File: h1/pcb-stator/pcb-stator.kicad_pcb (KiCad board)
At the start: 2 copper layers, 92.7 x 126.3 mm, 1646 parts, among them J1 Conn_01x01_Pin

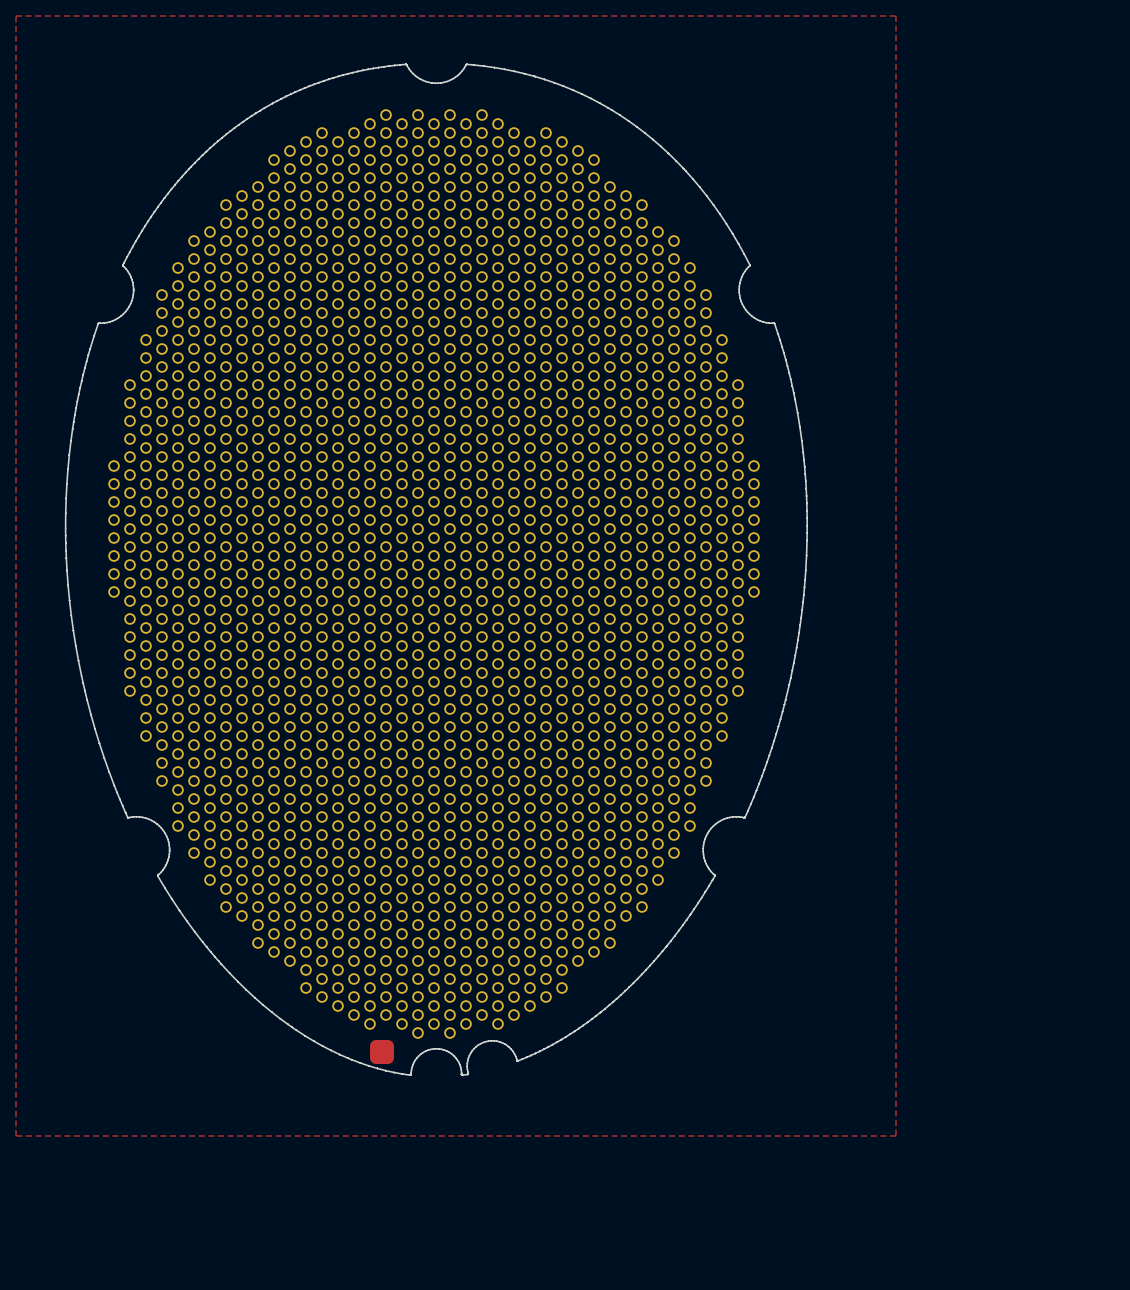
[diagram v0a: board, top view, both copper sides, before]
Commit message: h1: fixed stator alignment
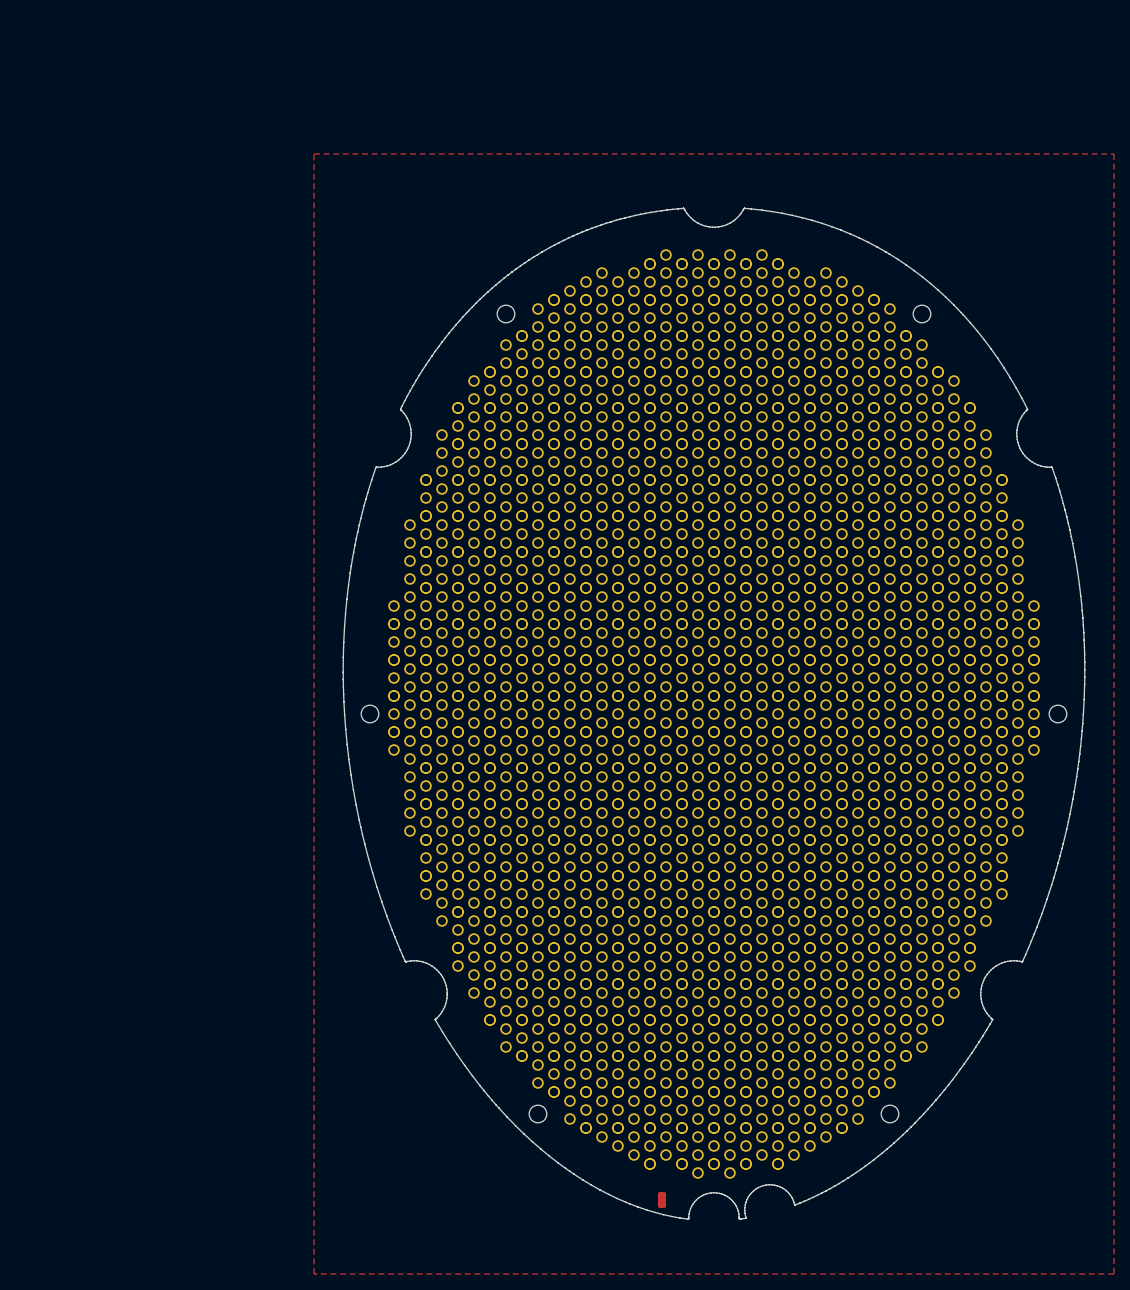
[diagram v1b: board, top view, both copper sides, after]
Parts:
- removed the ? at (41.0, 69.0)
- removed the ? at (81.0, 105.0)
- removed the ? at (45.0, 89.2)
- removed the ? at (67.0, 70.1)
- removed the ? at (37.0, 78.0)
- removed the ? at (71.0, 106.1)
- removed the ? at (37.0, 80.2)
- removed the ? at (45.0, 33.0)
- removed the ? at (73.0, 125.2)
- removed the ? at (77.0, 80.2)
- removed the ? at (65.0, 26.2)
- removed the ? at (49.0, 69.0)
- removed the ? at (61.0, 60.0)
- removed the ? at (61.0, 71.2)
- removed the ? at (73.0, 132.0)
- removed the ? at (61.0, 132.0)
- removed the ? at (91.0, 70.1)
- removed the ? at (81.0, 62.2)
- removed the ? at (95.0, 67.9)
- removed the ? at (59.0, 94.9)
- removed the ? at (41.0, 44.2)
- removed the ? at (81.0, 98.2)
- removed the ? at (55.0, 40.9)
- removed the ? at (61.0, 80.2)
- removed the ? at (63.0, 49.9)
- removed the ? at (93.0, 71.2)
- removed the ? at (91.0, 58.9)
- removed the ? at (89.0, 80.2)
- removed the ? at (55.0, 85.9)
- removed the ? at (59.0, 124.1)
- removed the ? at (39.0, 79.1)
- removed the ? at (77.0, 107.2)
- removed the ? at (67.0, 31.9)
- removed the ? at (37.0, 116.2)
- removed the ? at (83.0, 130.9)
- removed the ? at (75.0, 121.9)
- removed the ? at (59.0, 67.9)
- removed the ? at (33.0, 96.0)
- removed the ? at (57.0, 80.2)
- removed the ? at (95.0, 52.1)
- removed the ? at (87.0, 124.1)
- removed the ? at (99.0, 61.1)
- removed the ? at (63.0, 43.1)
- removed the ? at (65.0, 53.2)
- removed the ? at (93.0, 87.0)
- removed the ? at (53.0, 44.2)
- removed the ? at (89.0, 62.2)
- removed the ? at (75.0, 58.9)
- removed the ? at (59.0, 103.9)
- removed the ? at (41.0, 51.0)
- removed the ? at (101.0, 69.0)
- removed the ? at (41.0, 80.2)
- removed the ? at (53.0, 51.0)
- removed the ? at (89.0, 123.0)
- removed the ? at (75.0, 61.1)
- removed the ? at (65.0, 132.0)
- removed the ? at (53.0, 78.0)
- removed the ? at (41.0, 62.2)
- removed the ? at (71.0, 76.9)
- removed the ? at (27.0, 67.9)
- removed the ? at (91.0, 94.9)
- removed the ? at (53.0, 134.2)
- removed the ? at (97.0, 78.0)
- removed the ? at (67.0, 124.1)
- removed the ? at (47.0, 88.1)
- removed the ? at (85.0, 78.0)
- removed the ? at (71.0, 34.1)
- removed the ? at (79.0, 76.9)
- removed the ? at (83.0, 34.1)
- removed the ? at (63.0, 88.1)
- removed the ? at (89.0, 96.0)
- removed the ? at (79.0, 121.9)
- removed the ? at (57.0, 116.2)
- removed the ? at (101.0, 96.0)
- removed the ? at (69.0, 42.0)
- removed the ? at (47.0, 97.1)
- removed the ? at (53.0, 87.0)
- removed the ? at (49.0, 53.2)
- removed the ? at (53.0, 107.2)
- removed the ? at (43.0, 115.1)
- removed the ? at (67.0, 133.1)
- removed the ? at (55.0, 115.1)
- removed the ? at (89.0, 89.2)
- removed the ? at (99.0, 52.1)
- removed the ? at (97.0, 62.2)
- removed the ? at (57.0, 44.2)
- removed the ? at (69.0, 71.2)
- removed the ? at (31.0, 49.9)
- removed the ? at (39.0, 115.1)
- removed the ? at (41.0, 123.0)
- removed the ? at (75.0, 97.1)
- removed the ? at (31.0, 70.1)
- removed the ? at (79.0, 49.9)
- removed the ? at (105.0, 80.2)
- removed the ? at (99.0, 70.1)
- removed the ? at (91.0, 52.1)
- removed the ? at (95.0, 94.9)
- removed the ? at (83.0, 79.1)
- removed the ? at (69.0, 132.0)
- removed the ? at (73.0, 51.0)
- removed the ? at (57.0, 51.0)
- removed the ? at (51.0, 79.1)
- removed the ? at (39.0, 106.1)
- removed the ? at (51.0, 112.9)
- removed the ? at (99.0, 67.9)
- removed the ? at (93.0, 116.2)
- removed the ? at (91.0, 40.9)
- removed the ? at (55.0, 34.1)
- removed the ? at (83.0, 112.9)
- removed the ? at (43.0, 49.9)
- removed the ? at (73.0, 78.0)
- removed the ? at (37.0, 105.0)
- removed the ? at (59.0, 43.1)
- removed the ? at (31.0, 103.9)
- removed the ? at (77.0, 78.0)
- removed the ? at (81.0, 132.0)
- removed the ? at (85.0, 62.2)
- removed the ? at (29.0, 71.2)
- removed the ? at (35.0, 85.9)
- removed the ? at (49.0, 123.0)
- removed the ? at (59.0, 34.1)
- removed the ? at (67.0, 61.1)
- removed the ? at (79.0, 97.1)
- removed the ? at (59.0, 121.9)
- removed the ? at (35.0, 52.1)
- removed the ? at (37.0, 60.0)
- removed the ? at (73.0, 134.2)
- removed the ? at (55.0, 52.1)
- removed the ? at (99.0, 76.9)
- removed the ? at (67.0, 112.9)
- removed the ? at (103.0, 88.1)
- removed the ? at (87.0, 49.9)
- removed the ? at (43.0, 34.1)
- removed the ? at (71.0, 25.1)
- removed the ? at (63.0, 40.9)
- removed the ? at (65.0, 42.0)
- removed the ? at (47.0, 61.1)
- removed the ? at (73.0, 98.2)
- removed the ? at (27.0, 76.9)
- removed the ? at (47.0, 52.1)
- removed the ? at (49.0, 35.2)
- removed the ? at (83.0, 49.9)
- removed the ? at (81.0, 53.2)
- removed the ? at (61.0, 105.0)
- removed the ? at (65.0, 78.0)
- removed the ? at (105.0, 78.0)
- removed the ? at (61.0, 69.0)
- removed the ? at (53.0, 105.0)
- removed the ? at (65.0, 116.2)
- removed the ? at (69.0, 44.2)
- removed the ? at (81.0, 107.2)
- removed the ? at (67.0, 139.9)
- removed the ? at (103.0, 79.1)
- removed the ? at (65.0, 123.0)
- removed the ? at (103.0, 85.9)
- removed the ? at (105.0, 69.0)
- removed the ? at (61.0, 35.2)
- removed the ? at (53.0, 125.2)
- removed the ? at (69.0, 35.2)
- removed the ? at (65.0, 51.0)
- removed the ? at (41.0, 71.2)
- removed the ? at (47.0, 106.1)
- removed the ? at (99.0, 85.9)
- removed the ? at (77.0, 51.0)
- removed the ? at (65.0, 62.2)
- removed the ? at (63.0, 76.9)
- removed the ? at (79.0, 79.1)
- removed the ? at (69.0, 69.0)
- removed the ? at (81.0, 69.0)
- removed the ? at (35.0, 88.1)
- removed the ? at (55.0, 94.9)
- removed the ? at (65.0, 114.0)
- removed the ? at (55.0, 43.1)
- removed the ? at (49.0, 116.2)
- removed the ? at (61.0, 78.0)
- removed the ? at (71.0, 70.1)
- removed the ? at (75.0, 76.9)
- removed the ? at (87.0, 121.9)
- removed the ? at (61.0, 96.0)
- removed the ? at (81.0, 33.0)
- removed the ? at (45.0, 69.0)
- removed the ? at (95.0, 88.1)
- removed the ? at (27.0, 79.1)
- removed the ? at (73.0, 123.0)
- removed the ? at (79.0, 112.9)
- removed the ? at (55.0, 61.1)
- removed the ? at (53.0, 71.2)
- removed the ? at (71.0, 61.1)
- removed the ? at (55.0, 133.1)
- removed the ? at (31.0, 58.9)
- removed the ? at (47.0, 34.1)
- removed the ? at (33.0, 44.2)
- removed the ? at (57.0, 123.0)
- removed the ? at (79.0, 115.1)
- removed the ? at (99.0, 106.1)
- removed the ? at (81.0, 89.2)
- removed the ? at (37.0, 69.0)
- removed the ? at (41.0, 60.0)
- removed the ? at (73.0, 89.2)
- removed the ? at (97.0, 89.2)
- removed the ? at (61.0, 53.2)
- removed the ? at (101.0, 71.2)
- removed the ? at (49.0, 78.0)
- removed the ? at (41.0, 35.2)
- removed the ? at (55.0, 121.9)
- removed the ? at (35.0, 106.1)
- removed the ? at (31.0, 94.9)
- removed the ? at (93.0, 114.0)
- removed the ? at (45.0, 51.0)
- removed the ? at (85.0, 42.0)
- removed the ? at (57.0, 132.0)
- removed the ? at (95.0, 49.9)
- removed the ? at (51.0, 130.9)
- removed the ? at (71.0, 124.1)
- removed the ? at (95.0, 97.1)
- removed the ? at (47.0, 112.9)
- removed the ? at (93.0, 80.2)
- removed the ? at (97.0, 60.0)
- removed the ? at (83.0, 94.9)
- removed the ? at (89.0, 35.2)
- removed the ? at (77.0, 105.0)
- removed the ? at (87.0, 88.1)
- removed the ? at (83.0, 121.9)
- removed the ? at (85.0, 87.0)
- removed the ? at (27.0, 58.9)
- removed the ? at (45.0, 87.0)
- removed the ? at (43.0, 121.9)
- removed the ? at (79.0, 34.1)
- removed the ? at (51.0, 121.9)
- removed the ? at (43.0, 106.1)
- removed the ? at (81.0, 116.2)
- removed the ? at (51.0, 34.1)
- removed the ? at (31.0, 106.1)
- removed the ? at (55.0, 58.9)
- removed the ? at (89.0, 69.0)
- removed the ? at (65.0, 80.2)
- removed the ? at (39.0, 103.9)
- removed the ? at (97.0, 107.2)
- removed the ? at (33.0, 107.2)
- removed the ? at (75.0, 43.1)
- removed the ? at (71.0, 85.9)
- removed the ? at (69.0, 125.2)
- removed the ? at (73.0, 44.2)
- removed the ? at (61.0, 107.2)
- removed the ? at (75.0, 52.1)
- removed the ? at (63.0, 97.1)
- removed the ? at (37.0, 62.2)
- removed the ? at (83.0, 31.9)
- removed the ? at (67.0, 106.1)
- removed the ? at (91.0, 112.9)
- removed the ? at (59.0, 58.9)
- removed the ? at (87.0, 67.9)
- removed the ? at (31.0, 85.9)
- removed the ? at (89.0, 44.2)
- removed the ? at (73.0, 69.0)
- removed the ? at (71.0, 67.9)
- removed the ? at (69.0, 107.2)
- removed the ? at (67.0, 79.1)
- removed the ? at (91.0, 43.1)
- removed the ? at (63.0, 31.9)
- removed the ? at (81.0, 44.2)
- removed the ? at (61.0, 98.2)
- removed the ? at (85.0, 105.0)
- removed the ? at (71.0, 121.9)
- removed the ? at (71.0, 40.9)
- removed the ? at (61.0, 116.2)
- removed the ? at (47.0, 130.9)
- removed the ? at (81.0, 71.2)
- removed the ? at (65.0, 35.2)
- removed the ? at (87.0, 112.9)
- removed the ? at (93.0, 105.0)
- removed the ? at (83.0, 43.1)
- removed the ? at (101.0, 87.0)
- removed the ? at (87.0, 52.1)
- removed the ? at (67.0, 40.9)
- removed the ? at (59.0, 115.1)
- removed the ? at (43.0, 79.1)
- removed the ? at (67.0, 103.9)
- removed the ? at (65.0, 60.0)
- removed the ? at (63.0, 58.9)
- removed the ? at (25.0, 78.0)
- removed the ? at (59.0, 79.1)
- removed the ? at (101.0, 80.2)
- removed the ? at (53.0, 89.2)
- removed the ? at (51.0, 61.1)
- removed the ? at (69.0, 89.2)
- removed the ? at (59.0, 31.9)
- removed the ? at (73.0, 105.0)
- removed the ? at (41.0, 114.0)
- removed the ? at (97.0, 53.2)
- removed the ? at (39.0, 88.1)
- removed the ? at (53.0, 60.0)
- removed the ? at (53.0, 42.0)
- removed the ? at (35.0, 79.1)
- removed the ? at (47.0, 43.1)
- removed the ? at (51.0, 94.9)
- removed the ? at (93.0, 60.0)
- removed the ? at (69.0, 78.0)
- removed the ? at (61.0, 87.0)
- removed the ? at (83.0, 70.1)
- removed the ? at (59.0, 40.9)
- removed the ? at (97.0, 96.0)
- removed the ? at (63.0, 103.9)
- removed the ? at (89.0, 42.0)
- removed the ? at (79.0, 61.1)
- removed the ? at (45.0, 71.2)
- removed the ? at (85.0, 71.2)
- removed the ? at (83.0, 67.9)
- removed the ? at (51.0, 124.1)
- removed the ? at (37.0, 89.2)
- removed the ? at (35.0, 40.9)
- removed the ? at (95.0, 106.1)
- removed the ? at (99.0, 94.9)
- removed the ? at (55.0, 49.9)
- removed the ? at (57.0, 105.0)
- removed the ? at (77.0, 123.0)
- removed the ? at (51.0, 49.9)
- removed the ? at (35.0, 76.9)
- removed the ? at (47.0, 94.9)
- removed the ? at (65.0, 98.2)
- removed the ? at (49.0, 107.2)
- removed the ? at (45.0, 60.0)
- removed the ? at (31.0, 61.1)
- removed the ? at (89.0, 71.2)
- removed the ? at (55.0, 67.9)
- removed the ? at (61.0, 125.2)
- removed the ? at (47.0, 85.9)
- removed the ? at (47.0, 121.9)
- removed the ? at (29.0, 53.2)
- removed the ? at (63.0, 112.9)
- removed the ? at (31.0, 52.1)
- removed the ? at (35.0, 97.1)
- removed the ? at (49.0, 44.2)
- removed the ? at (59.0, 133.1)
- removed the ? at (51.0, 88.1)
- removed the ? at (97.0, 51.0)
- removed the ? at (27.0, 61.1)
- removed the ? at (43.0, 85.9)
- removed the ? at (29.0, 62.2)
- removed the ? at (73.0, 60.0)
- removed the ? at (57.0, 26.2)
- removed the ? at (91.0, 61.1)
- removed the ? at (81.0, 134.2)
- removed the ? at (77.0, 62.2)
- removed the ? at (69.0, 60.0)
- removed the ? at (43.0, 40.9)
- removed the ? at (39.0, 94.9)
- removed the ? at (41.0, 89.2)
- removed the ? at (69.0, 26.2)
- removed the ? at (31.0, 88.1)
- removed the ? at (95.0, 61.1)
- removed the ? at (33.0, 114.0)
- removed the ? at (73.0, 116.2)
- removed the ? at (91.0, 79.1)
- removed the ? at (91.0, 67.9)
- removed the ? at (53.0, 69.0)
- removed the ? at (51.0, 43.1)
- removed the ? at (59.0, 112.9)
- removed the ? at (97.0, 87.0)
- removed the ? at (49.0, 98.2)
- removed the ? at (83.0, 40.9)
- removed the ? at (55.0, 103.9)
- removed the ? at (53.0, 116.2)
- removed the ? at (33.0, 87.0)
- removed the ? at (61.0, 51.0)
- removed the ? at (69.0, 116.2)
- removed the ? at (71.0, 94.9)
- removed the ? at (89.0, 114.0)
- removed the ? at (49.0, 134.2)
- removed the ? at (91.0, 97.1)
- removed the ? at (35.0, 70.1)
- removed the ? at (83.0, 106.1)
- removed the ? at (45.0, 107.2)
- removed the ? at (51.0, 97.1)
- removed the ? at (51.0, 52.1)
- removed the ? at (71.0, 133.1)
- removed the ? at (99.0, 58.9)
- removed the ? at (29.0, 98.2)
- removed the ? at (65.0, 69.0)
- removed the ? at (51.0, 58.9)
- removed the ? at (45.0, 53.2)
- removed the ? at (83.0, 52.1)
- removed the ? at (91.0, 121.9)
- removed the ? at (39.0, 112.9)
- removed the ? at (103.0, 70.1)
- removed the ? at (53.0, 98.2)
- removed the ? at (75.0, 130.9)
- removed the ? at (85.0, 51.0)
- removed the ? at (101.0, 98.2)
- removed the ? at (69.0, 80.2)
- removed the ? at (39.0, 61.1)
- removed the ? at (53.0, 114.0)
- removed the ? at (65.0, 71.2)
- removed the ? at (69.0, 105.0)
- removed the ? at (47.0, 70.1)
- removed the ? at (91.0, 106.1)
- removed the ? at (65.0, 89.2)
- removed the ? at (41.0, 96.0)
- removed the ? at (57.0, 53.2)
- removed the ? at (37.0, 42.0)
- removed the ? at (95.0, 70.1)
- removed the ? at (103.0, 61.1)
- removed the ? at (103.0, 76.9)
- removed the ? at (79.0, 103.9)
- removed the ? at (75.0, 79.1)
- removed the ? at (99.0, 79.1)
- removed the ? at (97.0, 105.0)
- removed the ? at (73.0, 35.2)
- removed the ? at (71.0, 49.9)
- removed the ? at (75.0, 103.9)
- removed the ? at (93.0, 107.2)
- removed the ? at (41.0, 107.2)
- removed the ? at (33.0, 62.2)
- removed the ? at (35.0, 67.9)
- removed the ? at (27.0, 94.9)
- removed the ? at (63.0, 115.1)
- removed the ? at (93.0, 44.2)
- removed the ? at (57.0, 62.2)
- removed the ? at (45.0, 105.0)
- removed the ? at (77.0, 87.0)
- removed the ? at (47.0, 58.9)
- removed the ? at (59.0, 88.1)
- removed the ? at (47.0, 76.9)
- removed the ? at (75.0, 133.1)
- removed the ? at (81.0, 78.0)
- removed the ? at (63.0, 52.1)
- removed the ? at (77.0, 134.2)
- removed the ? at (67.0, 130.9)
- removed the ? at (85.0, 80.2)
- removed the ? at (99.0, 97.1)
- removed the ? at (69.0, 62.2)
- removed the ? at (61.0, 42.0)
- removed the ? at (63.0, 106.1)
- removed the ? at (33.0, 105.0)
- removed the ? at (59.0, 52.1)
- removed the ? at (83.0, 97.1)
- removed the ? at (39.0, 43.1)
- removed the ? at (79.0, 52.1)
- removed the ? at (37.0, 44.2)
- removed the ? at (93.0, 42.0)
- removed the ? at (39.0, 49.9)
- removed the ? at (55.0, 112.9)
- removed the ? at (95.0, 43.1)
- removed the ? at (79.0, 124.1)
- removed the ? at (69.0, 51.0)
- removed the ? at (63.0, 70.1)
- removed the ? at (63.0, 34.1)
- removed the ? at (43.0, 61.1)
- removed the ? at (31.0, 79.1)
- removed the ? at (67.0, 115.1)
- removed the ? at (103.0, 58.9)
- removed the ? at (97.0, 98.2)
- removed the ? at (33.0, 98.2)
- removed the ? at (65.0, 105.0)
- removed the ? at (53.0, 80.2)
- removed the ? at (79.0, 31.9)
- removed the ? at (87.0, 79.1)
- removed the ? at (39.0, 85.9)
- removed the ? at (45.0, 98.2)
- removed the ? at (75.0, 106.1)
- removed the ? at (85.0, 33.0)
- removed the ? at (87.0, 115.1)
- removed the ? at (71.0, 130.9)
- removed the ? at (67.0, 43.1)
- removed the ? at (49.0, 42.0)
- removed the ? at (51.0, 40.9)
- removed the ? at (57.0, 98.2)
- removed the ? at (69.0, 96.0)
- removed the ? at (85.0, 96.0)
- removed the ? at (97.0, 71.2)
- removed the ? at (87.0, 61.1)
- removed the ? at (49.0, 51.0)
- removed the ? at (79.0, 40.9)
- removed the ? at (73.0, 107.2)
- removed the ? at (67.0, 76.9)
- removed the ? at (67.0, 121.9)
- removed the ? at (49.0, 89.2)
- removed the ? at (43.0, 67.9)
- removed the ? at (101.0, 60.0)
- removed the ? at (51.0, 31.9)
- removed the ? at (53.0, 62.2)
- removed the ? at (93.0, 53.2)
- removed the ? at (49.0, 96.0)
- removed the ? at (93.0, 69.0)
- removed the ? at (83.0, 88.1)
- removed the ? at (67.0, 52.1)
- removed the ? at (99.0, 49.9)
- removed the ? at (63.0, 67.9)
- removed the ? at (71.0, 52.1)
- removed the ? at (87.0, 103.9)
- removed the ? at (85.0, 107.2)
- removed the ? at (87.0, 76.9)
- removed the ? at (97.0, 114.0)
- removed the ? at (71.0, 112.9)
- removed the ? at (57.0, 33.0)
- removed the ? at (41.0, 116.2)
- removed the ? at (53.0, 53.2)
- removed the ? at (69.0, 123.0)
- removed the ? at (83.0, 85.9)
- removed the ? at (79.0, 67.9)
- removed the ? at (49.0, 132.0)
- removed the ? at (47.0, 31.9)
- removed the ? at (87.0, 85.9)
- removed the ? at (79.0, 58.9)
- removed the ? at (65.0, 96.0)
- removed the ? at (85.0, 69.0)
- removed the ? at (77.0, 44.2)
- removed the ? at (47.0, 124.1)
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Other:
- outline, holes or cut-outs redrawn

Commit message: h1: fixed stator & spacer edge cuts
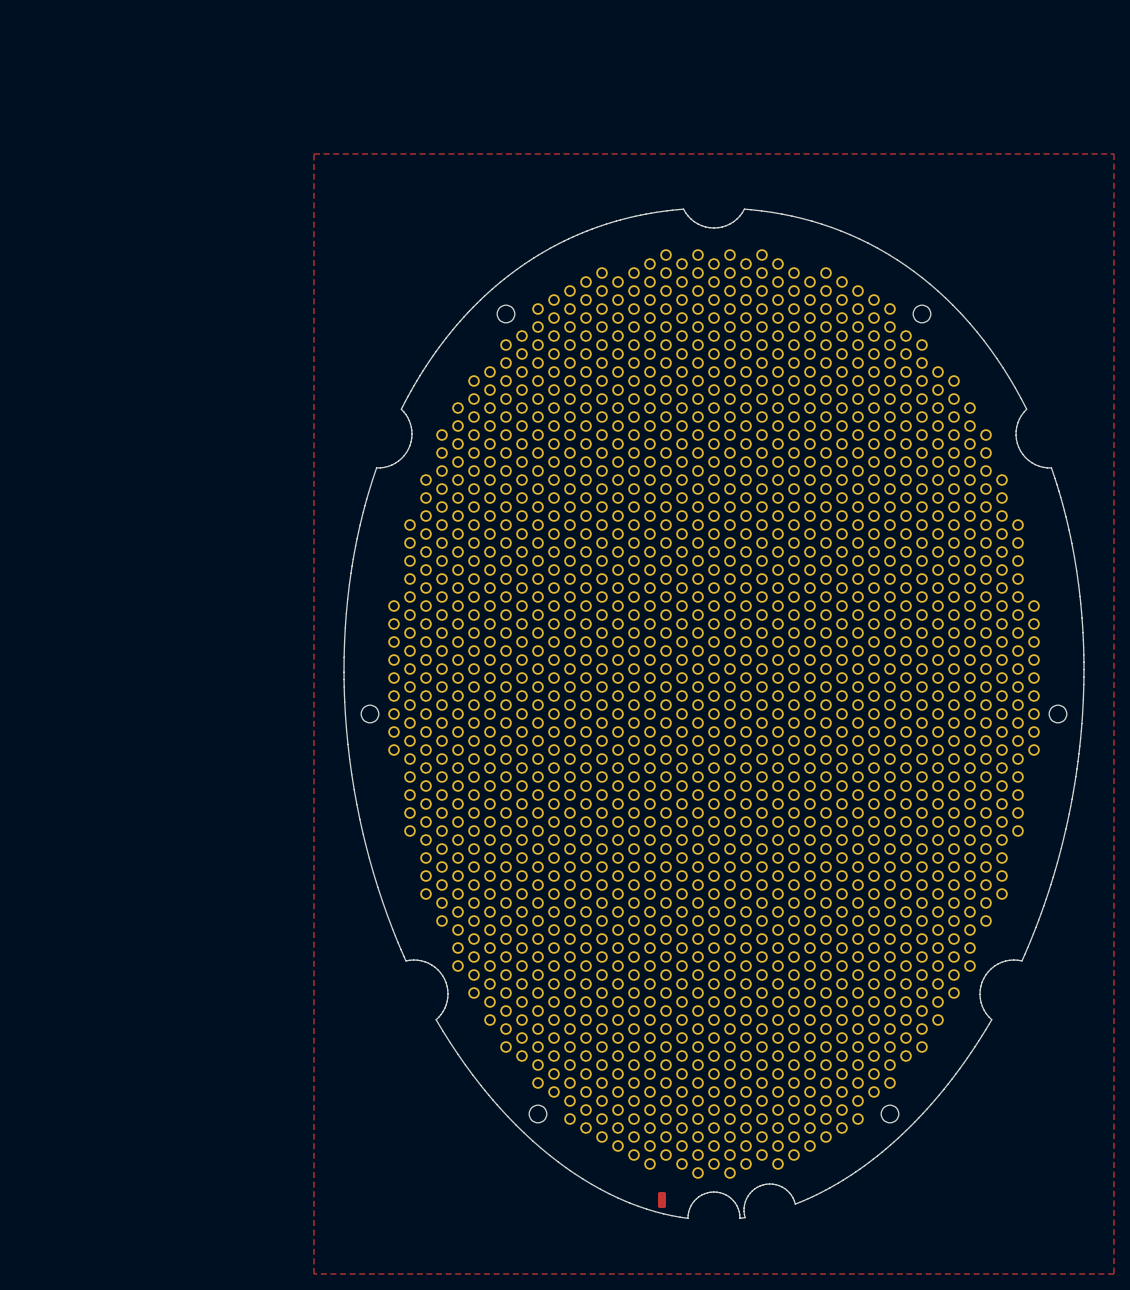
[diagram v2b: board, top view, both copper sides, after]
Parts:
- removed ? (x416): , 
- removed the REF** at (82.0, 121.4)
- removed the REF** at (92.0, 124.8)
- removed the REF** at (84.0, 95.5)
- removed the REF** at (104.0, 68.5)
- removed the REF** at (112.0, 151.8)
- removed the REF** at (114.0, 98.9)
- removed the REF** at (118.0, 76.4)
- removed the REF** at (98.0, 116.9)
- removed the REF** at (98.0, 101.1)
- removed the REF** at (102.0, 114.6)
- removed the REF** at (122.0, 80.9)
- removed the REF** at (134.0, 94.4)
- removed the REF** at (114.0, 116.9)
- removed the REF** at (98.0, 71.9)
- removed the REF** at (132.0, 127.0)
- removed the REF** at (132.0, 77.5)
- removed the REF** at (100.0, 129.2)
- removed the REF** at (118.0, 49.4)
- removed the REF** at (84.0, 75.2)
- removed the REF** at (120.0, 55.0)
- removed the REF** at (80.0, 61.8)
- removed the REF** at (116.0, 86.5)
- removed the REF** at (120.0, 145.0)
- removed the REF** at (70.0, 132.6)
- removed the REF** at (98.0, 121.4)
- removed the REF** at (116.0, 120.2)
- removed the REF** at (122.0, 51.6)
- removed the REF** at (106.0, 130.4)
- removed the REF** at (94.0, 141.6)
- removed the REF** at (70.0, 69.6)
- removed the REF** at (116.0, 124.8)
- removed the REF** at (130.0, 96.6)
- removed the REF** at (114.0, 137.1)
- removed the REF** at (126.0, 67.4)
- removed the REF** at (110.0, 155.1)
- removed the REF** at (136.0, 118.0)
- removed the REF** at (126.0, 98.9)
- removed the REF** at (110.0, 89.9)
- removed the REF** at (116.0, 151.8)
- removed the REF** at (68.0, 106.8)
- removed the REF** at (100.0, 102.2)
- removed the REF** at (96.0, 50.5)
- removed the REF** at (114.0, 89.9)
- removed the REF** at (112.0, 61.8)
- removed the REF** at (128.0, 64.0)
- removed the REF** at (86.0, 110.1)
- removed the REF** at (80.0, 64.0)
- removed the REF** at (88.0, 77.5)
- removed the REF** at (78.0, 83.1)
- removed the REF** at (118.0, 103.4)
- removed the REF** at (80.0, 133.8)
- removed the REF** at (124.0, 70.8)
- removed the REF** at (94.0, 42.6)
- removed the REF** at (108.0, 156.2)
- removed the REF** at (118.0, 87.6)
- removed the REF** at (64.0, 73.0)
- removed the REF** at (106.0, 121.4)
- removed the REF** at (118.0, 125.9)
- removed the REF** at (82.0, 65.1)
- removed the REF** at (66.0, 121.4)
- removed the REF** at (84.0, 127.0)
- removed the REF** at (122.0, 71.9)
- removed the REF** at (88.0, 97.8)
- removed the REF** at (104.0, 95.5)
- removed the REF** at (80.0, 50.5)
- removed the REF** at (96.0, 104.5)
- removed the REF** at (132.0, 118.0)
- removed the REF** at (80.0, 145.0)
- removed the REF** at (140.0, 95.5)
- removed the REF** at (120.0, 97.8)
- removed the REF** at (76.0, 91.0)
- removed the REF** at (112.0, 48.2)
- removed the REF** at (116.0, 88.8)
- removed the REF** at (104.0, 79.8)
- removed the REF** at (76.0, 52.8)
- removed the REF** at (138.0, 103.4)
- removed the REF** at (128.0, 129.2)
- removed the REF** at (98.0, 47.1)
- removed the REF** at (80.0, 79.8)
- removed the REF** at (108.0, 136.0)
- removed the REF** at (128.0, 97.8)
- removed the REF** at (102.0, 150.6)
- removed the REF** at (96.0, 52.8)
- removed the REF** at (76.0, 61.8)
- removed the REF** at (130.0, 76.4)
- removed the REF** at (98.0, 74.1)
- removed the REF** at (112.0, 70.8)
- removed the REF** at (110.0, 51.6)
- removed the REF** at (136.0, 86.5)
- removed the REF** at (74.0, 101.1)
- removed the REF** at (106.0, 85.4)
- removed the REF** at (118.0, 137.1)
- removed the REF** at (100.0, 133.8)
- removed the REF** at (94.0, 80.9)
- removed the REF** at (122.0, 69.6)
- removed the REF** at (104.0, 124.8)
- removed the REF** at (130.0, 78.6)
- removed the REF** at (84.0, 93.2)
- removed the REF** at (84.0, 100.0)
- removed the REF** at (64.0, 77.5)
- removed the REF** at (90.0, 47.1)
- removed the REF** at (106.0, 152.9)
- removed the REF** at (100.0, 95.5)
- removed the REF** at (104.0, 102.2)
- removed the REF** at (92.0, 129.2)
- removed the REF** at (92.0, 59.5)
- removed the REF** at (96.0, 115.8)
- removed the REF** at (100.0, 111.2)
- removed the REF** at (112.0, 102.2)
- removed the REF** at (106.0, 87.6)
- removed the REF** at (114.0, 141.6)
- removed the REF** at (66.0, 107.9)
- removed the REF** at (112.0, 77.5)
- removed the REF** at (114.0, 58.4)
- removed the REF** at (134.0, 92.1)
- removed the REF** at (94.0, 132.6)
- removed the REF** at (66.0, 112.4)
- removed the REF** at (122.0, 98.9)
- removed the REF** at (122.0, 101.1)
- removed the REF** at (80.0, 95.5)
- removed the REF** at (122.0, 141.6)
- removed the REF** at (124.0, 52.8)
- removed the REF** at (128.0, 100.0)
- removed the REF** at (104.0, 75.2)
- removed the REF** at (90.0, 94.4)
- removed the REF** at (68.0, 66.2)
- removed the REF** at (138.0, 96.6)
- removed the REF** at (112.0, 145.0)
- removed the REF** at (78.0, 121.4)
- removed the REF** at (106.0, 119.1)
- removed the REF** at (134.0, 85.4)
- removed the REF** at (84.0, 142.8)
- removed the REF** at (116.0, 140.5)
- removed the REF** at (138.0, 87.6)
- removed the REF** at (76.0, 93.2)
- removed the REF** at (76.0, 77.5)
- removed the REF** at (98.0, 87.6)
- removed the REF** at (78.0, 65.1)
- removed the REF** at (82.0, 132.6)
- removed the REF** at (88.0, 106.8)
- removed the REF** at (114.0, 112.4)
- removed the REF** at (94.0, 74.1)
- removed the REF** at (110.0, 105.6)
- removed the REF** at (110.0, 143.9)
- removed the REF** at (102.0, 137.1)
- removed the REF** at (108.0, 95.5)
- removed the REF** at (86.0, 96.6)
- removed the REF** at (102.0, 107.9)
- removed the REF** at (106.0, 134.9)
- removed the REF** at (140.0, 100.0)
- removed the REF** at (100.0, 147.2)
- removed the REF** at (100.0, 68.5)
- removed the REF** at (126.0, 80.9)
- removed the REF** at (76.0, 111.2)
- removed the REF** at (102.0, 67.4)
- removed the REF** at (92.0, 147.2)
- removed the REF** at (88.0, 145.0)
- removed the REF** at (84.0, 70.8)
- removed the REF** at (90.0, 139.4)
- removed the REF** at (128.0, 102.2)
- removed the REF** at (106.0, 53.9)
- removed the REF** at (136.0, 102.2)
- removed the REF** at (96.0, 100.0)
- removed the REF** at (140.0, 97.8)
- removed the REF** at (104.0, 145.0)
- removed the REF** at (130.0, 123.6)
- removed the REF** at (102.0, 51.6)
- removed the REF** at (86.0, 101.1)
- removed the REF** at (68.0, 113.5)
- removed the REF** at (120.0, 61.8)
- removed the REF** at (80.0, 86.5)
- removed the REF** at (106.0, 58.4)
- removed the REF** at (106.0, 94.4)
- removed the REF** at (108.0, 57.2)
- removed the REF** at (118.0, 74.1)
- removed the REF** at (78.0, 60.6)
- removed the REF** at (92.0, 113.5)
- removed the REF** at (134.0, 98.9)
- removed the REF** at (74.0, 87.6)
- removed the REF** at (114.0, 51.6)
- removed the REF** at (92.0, 151.8)
- removed the REF** at (74.0, 112.4)
- removed the REF** at (126.0, 101.1)
- removed the REF** at (108.0, 88.8)
- removed the REF** at (90.0, 130.4)
- removed the REF** at (116.0, 93.2)
- removed the REF** at (86.0, 94.4)
- removed the REF** at (104.0, 127.0)
- removed the REF** at (120.0, 68.5)
- removed the REF** at (96.0, 93.2)
- removed the REF** at (82.0, 85.4)
- removed the REF** at (92.0, 79.8)
- removed the REF** at (120.0, 75.2)
- removed the REF** at (94.0, 87.6)
- removed the REF** at (106.0, 65.1)
- removed the REF** at (88.0, 46.0)
- removed the REF** at (100.0, 142.8)
- removed the REF** at (104.0, 77.5)
- removed the REF** at (72.0, 88.8)
- removed the REF** at (76.0, 138.2)
- removed the REF** at (86.0, 112.4)
- removed the REF** at (130.0, 121.4)
- removed the REF** at (112.0, 113.5)
- removed the REF** at (90.0, 44.9)
- removed the REF** at (68.0, 75.2)
- removed the REF** at (98.0, 132.6)
- removed the REF** at (88.0, 55.0)
- removed the REF** at (120.0, 79.8)
- removed the REF** at (116.0, 109.0)
- removed the REF** at (78.0, 67.4)
- removed the REF** at (70.0, 60.6)
- removed the REF** at (102.0, 110.1)
- removed the REF** at (62.0, 76.4)
- removed the REF** at (104.0, 43.8)
- removed the REF** at (80.0, 147.2)
- removed the REF** at (112.0, 68.5)
- removed the REF** at (82.0, 76.4)
- removed the REF** at (88.0, 50.5)
- removed the REF** at (126.0, 128.1)
- removed the REF** at (90.0, 56.1)
- removed the REF** at (104.0, 136.0)
- removed the REF** at (84.0, 131.5)
- removed the REF** at (62.0, 105.6)
- removed the REF** at (104.0, 113.5)
- removed the REF** at (72.0, 118.0)
- removed the REF** at (108.0, 151.8)
- removed the REF** at (102.0, 134.9)
- removed the REF** at (120.0, 86.5)
- removed the REF** at (118.0, 112.4)
- removed the REF** at (128.0, 131.5)
- removed the REF** at (120.0, 133.8)
- removed the REF** at (124.0, 55.0)
- removed the REF** at (108.0, 102.2)
- removed the REF** at (74.0, 98.9)
- removed the REF** at (62.0, 78.6)
- removed the REF** at (98.0, 150.6)
- removed the REF** at (130.0, 103.4)
- removed the REF** at (132.0, 93.2)
- removed the REF** at (112.0, 106.8)
- removed the REF** at (110.0, 53.9)
- removed the REF** at (116.0, 70.8)
- removed the REF** at (90.0, 96.6)
- removed the REF** at (112.0, 73.0)
- removed the REF** at (76.0, 118.0)
- removed the REF** at (120.0, 93.2)
- removed the REF** at (122.0, 137.1)
- removed the REF** at (90.0, 132.6)
- removed the REF** at (96.0, 133.8)
- removed the REF** at (126.0, 139.4)
- removed the REF** at (70.0, 128.1)
- removed the REF** at (128.0, 57.2)
- removed the REF** at (140.0, 88.8)
- removed the REF** at (68.0, 61.8)
- removed the REF** at (92.0, 140.5)
- removed the REF** at (62.0, 114.6)
- removed the REF** at (82.0, 49.4)
- removed the REF** at (110.0, 58.4)
- removed the REF** at (118.0, 123.6)
- removed the REF** at (72.0, 95.5)
- removed the REF** at (136.0, 84.2)
- removed the REF** at (104.0, 109.0)
- removed the REF** at (100.0, 97.8)
- removed the REF** at (110.0, 98.9)
- removed the REF** at (76.0, 127.0)
- removed the REF** at (114.0, 65.1)
- removed the REF** at (98.0, 112.4)
- removed the REF** at (116.0, 142.8)
- removed the REF** at (102.0, 116.9)
- removed the REF** at (114.0, 121.4)
- removed the REF** at (84.0, 140.5)
- removed the REF** at (76.0, 129.2)
- removed the REF** at (74.0, 62.9)
- removed the REF** at (98.0, 78.6)
- removed the REF** at (140.0, 93.2)
- removed the REF** at (70.0, 94.4)
- removed the REF** at (70.0, 92.1)
- removed the REF** at (100.0, 77.5)
- removed the REF** at (100.0, 136.0)
- removed the REF** at (114.0, 53.9)
- removed the REF** at (108.0, 142.8)
- removed the REF** at (126.0, 125.9)
- removed the REF** at (68.0, 104.5)
- removed the REF** at (124.0, 115.8)
- removed the REF** at (86.0, 80.9)
- removed the REF** at (106.0, 146.1)
- removed the REF** at (130.0, 71.9)
- removed the REF** at (102.0, 119.1)
- removed the REF** at (78.0, 112.4)
- removed the REF** at (126.0, 83.1)
- removed the REF** at (80.0, 82.0)
- removed the REF** at (120.0, 136.0)
- removed the REF** at (94.0, 105.6)
- removed the REF** at (84.0, 84.2)
- removed the REF** at (100.0, 52.8)
- removed the REF** at (130.0, 83.1)
- removed the REF** at (94.0, 92.1)
- removed the REF** at (100.0, 46.0)
- removed the REF** at (104.0, 100.0)
- removed the REF** at (102.0, 130.4)
- removed the REF** at (112.0, 104.5)
- removed the REF** at (136.0, 82.0)
- removed the REF** at (96.0, 154.0)
- removed the REF** at (114.0, 130.4)
- removed the REF** at (108.0, 43.8)
- removed the REF** at (92.0, 149.5)
- removed the REF** at (86.0, 92.1)
- removed the REF** at (92.0, 52.8)
- removed the REF** at (80.0, 109.0)
- removed the REF** at (112.0, 86.5)
- removed the REF** at (118.0, 119.1)
- removed the REF** at (76.0, 59.5)
- removed the REF** at (102.0, 105.6)
- removed the REF** at (66.0, 80.9)
- removed the REF** at (78.0, 78.6)
- removed the REF** at (96.0, 151.8)
- removed the REF** at (68.0, 120.2)
- removed the REF** at (74.0, 130.4)
- removed the REF** at (100.0, 43.8)
- removed the REF** at (92.0, 68.5)
- removed the REF** at (104.0, 120.2)
- removed the REF** at (112.0, 140.5)
- removed the REF** at (120.0, 115.8)
- removed the REF** at (74.0, 78.6)
- removed the REF** at (74.0, 56.1)
- removed the REF** at (82.0, 141.6)
- removed the REF** at (94.0, 56.1)
- removed the REF** at (100.0, 55.0)
- removed the REF** at (92.0, 57.2)
- removed the REF** at (120.0, 106.8)
- removed the REF** at (130.0, 128.1)
- removed the REF** at (94.0, 98.9)
- removed the REF** at (112.0, 122.5)
- removed the REF** at (122.0, 96.6)
- removed the REF** at (132.0, 91.0)
- removed the REF** at (86.0, 74.1)
- removed the REF** at (112.0, 127.0)
- removed the REF** at (126.0, 76.4)
- removed the REF** at (92.0, 73.0)
- removed the REF** at (94.0, 103.4)
- removed the REF** at (82.0, 103.4)
- removed the REF** at (108.0, 149.5)
- removed the REF** at (102.0, 83.1)
- removed the REF** at (138.0, 112.4)
- removed the REF** at (74.0, 71.9)
- removed the REF** at (116.0, 100.0)
- removed the REF** at (88.0, 73.0)
- removed the REF** at (130.0, 89.9)
- removed the REF** at (60.0, 93.2)
- removed the REF** at (108.0, 64.0)
- removed the REF** at (104.0, 84.2)
- removed the REF** at (104.0, 149.5)
- removed the REF** at (134.0, 110.1)
- removed the REF** at (136.0, 100.0)
- removed the REF** at (124.0, 106.8)
- removed the REF** at (116.0, 68.5)
- removed the REF** at (88.0, 142.8)
- removed the REF** at (102.0, 112.4)
- removed the REF** at (86.0, 103.4)
- removed the REF** at (92.0, 64.0)
- removed the REF** at (94.0, 143.9)
- removed the REF** at (132.0, 111.2)
- removed the REF** at (88.0, 57.2)
- removed the REF** at (134.0, 125.9)
- removed the REF** at (78.0, 130.4)
- removed the REF** at (108.0, 140.5)
- removed the REF** at (114.0, 152.9)
- removed the REF** at (94.0, 110.1)
- removed the REF** at (134.0, 78.6)
- removed the REF** at (128.0, 59.5)
- removed the REF** at (78.0, 69.6)
- removed the REF** at (86.0, 83.1)
- removed the REF** at (96.0, 68.5)
- removed the REF** at (72.0, 124.8)
- removed the REF** at (128.0, 127.0)
- removed the REF** at (92.0, 118.0)
- removed the REF** at (136.0, 93.2)
- removed the REF** at (90.0, 51.6)
- removed the REF** at (118.0, 132.6)
- removed the REF** at (96.0, 70.8)
- removed the REF** at (94.0, 89.9)
- removed the REF** at (134.0, 112.4)
- removed the REF** at (100.0, 106.8)
- removed the REF** at (104.0, 57.2)
- removed the REF** at (136.0, 109.0)
- removed the REF** at (106.0, 74.1)
- removed the REF** at (114.0, 110.1)
- removed the REF** at (122.0, 78.6)
- removed the REF** at (80.0, 136.0)
- removed the REF** at (86.0, 123.6)
- removed the REF** at (128.0, 118.0)
- removed the REF** at (94.0, 146.1)
- removed the REF** at (86.0, 49.4)
- removed the REF** at (78.0, 87.6)
- removed the REF** at (116.0, 131.5)
- removed the REF** at (70.0, 87.6)
- removed the REF** at (118.0, 53.9)
- removed the REF** at (108.0, 68.5)
- removed the REF** at (104.0, 111.2)
- removed the REF** at (76.0, 140.5)
- removed the REF** at (126.0, 107.9)
- removed the REF** at (120.0, 70.8)
- removed the REF** at (86.0, 58.4)
- removed the REF** at (124.0, 88.8)
- removed the REF** at (84.0, 50.5)
- removed the REF** at (66.0, 101.1)
- removed the REF** at (92.0, 75.2)
- removed the REF** at (64.0, 95.5)
- removed the REF** at (74.0, 85.4)
- removed the REF** at (136.0, 77.5)
- removed the REF** at (82.0, 119.1)
- removed the REF** at (98.0, 58.4)
- removed the REF** at (82.0, 116.9)
- removed the REF** at (124.0, 79.8)
- removed the REF** at (64.0, 93.2)
- removed the REF** at (86.0, 125.9)
- removed the REF** at (110.0, 62.9)
- removed the REF** at (82.0, 146.1)
- removed the REF** at (66.0, 98.9)
- removed the REF** at (110.0, 49.4)
- removed the REF** at (66.0, 123.6)
- removed the REF** at (116.0, 104.5)
- removed the REF** at (90.0, 60.6)
- removed the REF** at (114.0, 92.1)
- removed the REF** at (80.0, 88.8)
- removed the REF** at (72.0, 109.0)
- removed the REF** at (92.0, 115.8)
- removed the REF** at (138.0, 83.1)
- removed the REF** at (98.0, 137.1)
- removed the REF** at (72.0, 64.0)
- removed the REF** at (132.0, 61.8)
- removed the REF** at (108.0, 61.8)
- removed the REF** at (114.0, 67.4)
- removed the REF** at (112.0, 147.2)
- removed the REF** at (132.0, 120.2)
- removed the REF** at (86.0, 87.6)
- removed the REF** at (124.0, 77.5)
- removed the REF** at (86.0, 143.9)
- removed the REF** at (102.0, 71.9)
- removed the REF** at (122.0, 125.9)
- removed the REF** at (106.0, 132.6)
- removed the REF** at (104.0, 73.0)
- removed the REF** at (82.0, 56.1)
- removed the REF** at (118.0, 114.6)
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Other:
- board size 92.7 x 126.3 mm -> 92.5 x 126.1 mm
